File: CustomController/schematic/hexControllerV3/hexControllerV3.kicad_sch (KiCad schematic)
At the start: 48 parts, among them IC1 ESP32-S2-MINI-1-N4R2, IC2 IP5306, J1 USB_C_Receptacle_USB2.0_16P, J2 Battery, J3 Switch1, J4 Switch2, J5 Switch3, J6 Switch4, J7 Battery, SW1 RotaryEncoder_Switch, SW2 SW_DIP_x01, SW3 SW_DIP_x01, SW4 SW_DIP_x01, SW5 SW_DIP_x01, SW6 SW_DIP_x01, U2 AMS1117-3.3

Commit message: Improved PCB design
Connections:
- net Switch1: now also IC1.19 (IO15); no longer IC1.18 (IO14)
- net Switch2: now also IC1.18 (IO14); no longer IC1.19 (IO15)
- net button1: now also IC1.33 (IO37)
- net button2: now also IC1.34 (IO38)
- net button3: now also IC1.35 (IO39)
- net button4: now also IC1.36 (IO40)
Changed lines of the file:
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@@
+		)
+	)
+	(global_label "button4"
+		(shape input)
+		(at 184.15 115.57 180)
+		(fields_autoplaced yes)
+		(effects
+			(font
+				(size 1.27 1.27)
+			)
+			(justify right)
+		)
+		(property "Intersheetrefs" "${INTERSHEET_REFS}"
+			(at 173.9079 115.57 0)
+			(effects
+				(font
+					(size 1.27 1.27)
+				)
+				(justify right)
+				(hide yes)
+			)
 		)
 	)
@@
 		)
 	)
+	(global_label "button2"
+		(shape input)
+		(at 184.15 110.49 180)
+		(fields_autoplaced yes)
+		(effects
+			(font
+				(size 1.27 1.27)
+			)
+			(justify right)
+		)
+		(property "Intersheetrefs" "${INTERSHEET_REFS}"
+			(at 173.9079 110.49 0)
+			(effects
+				(font
+					(size 1.27 1.27)
+				)
+				(justify right)
+				(hide yes)
+			)
+		)
+	)
 	(global_label "Switch3"
 		(shape input)
@@
 		)
 	)
+	(global_label "button3"
+		(shape input)
+		(at 184.15 113.03 180)
+		(fields_autoplaced yes)
+		(effects
+			(font
+				(size 1.27 1.27)
+			)
+			(justify right)
+		)
+		(property "Intersheetrefs" "${INTERSHEET_REFS}"
+			(at 173.9079 113.03 0)
+			(effects
+				(font
+					(size 1.27 1.27)
+				)
+				(justify right)
+				(hide yes)
+			)
+		)
+	)
 	(global_label "DIN"
 		(shape input)
@@
 		)
 	)
+	(global_label "button1"
+		(shape input)
+		(at 184.15 107.95 180)
+		(fields_autoplaced yes)
+		(effects
+			(font
+				(size 1.27 1.27)
+			)
+			(justify right)
+		)
+		(property "Intersheetrefs" "${INTERSHEET_REFS}"
+			(at 173.9079 107.95 0)
+			(effects
+				(font
+					(size 1.27 1.27)
+				)
+				(justify right)
+				(hide yes)
+			)
+		)
+	)
 	(global_label "D-"
 		(shape input)
@@
 	(global_label "Switch2"
 		(shape input)
+		(at 172.72 69.85 180)
+		(fields_autoplaced yes)
+		(effects
+			(font
+				(size 1.27 1.27)
+			)
+			(justify right)
+		)
+		(property "Intersheetrefs" "${INTERSHEET_REFS}"
+			(at 162.4172 69.85 0)
+			(effects
+				(font
+					(size 1.27 1.27)
+				)
+				(justify right)
+				(hide yes)
+			)
+		)
+	)
+	(global_label "EncoderSW"
+		(shape input)
+		(at 157.48 52.07 180)
+		(fields_autoplaced yes)
+		(effects
+			(font
+				(size 1.27 1.27)
+			)
+			(justify right)
+		)
+		(property "Intersheetrefs" "${INTERSHEET_REFS}"
+			(at 145.8468 52.07 0)
+			(effects
+				(font
+					(size 1.27 1.27)
+				)
+				(justify right)
+				(hide yes)
+			)
+		)
+	)
+	(global_label "BOOT"
+		(shape input)
+		(at 184.15 34.29 180)
+		(fields_autoplaced yes)
+		(effects
+			(font
+				(size 1.27 1.27)
+			)
+			(justify right)
+		)
+		(property "Intersheetrefs" "${INTERSHEET_REFS}"
+			(at 176.2662 34.29 0)
+			(effects
+				(font
+					(size 1.27 1.27)
+				)
+				(justify right)
+				(hide yes)
+			)
+		)
+	)
+	(global_label "Joy1Y"
+		(shape input)
+		(at 158.75 36.83 180)
+		(fields_autoplaced yes)
+		(effects
+			(font
+				(size 1.27 1.27)
+			)
+			(justify right)
+		)
+		(property "Intersheetrefs" "${INTERSHEET_REFS}"
+			(at 150.2616 36.83 0)
+			(effects
+				(font
+					(size 1.27 1.27)
+				)
+				(justify right)
+				(hide yes)
+			)
+		)
+	)
+	(global_label "Joy1X"
+		(shape input)
+		(at 158.75 39.37 180)
+		(fields_autoplaced yes)
+		(effects
+			(font
+				(size 1.27 1.27)
+			)
+			(justify right)
+		)
+		(property "Intersheetrefs" "${INTERSHEET_REFS}"
+			(at 150.3825 39.37 0)
+			(effects
+				(font
+					(size 1.27 1.27)
+				)
+				(justify right)
+				(hide yes)
+			)
+		)
+	)
+	(global_label "EN"
+		(shape input)
+		(at 59.69 256.54 180)
+		(fields_autoplaced yes)
+		(effects
+			(font
+				(size 1.27 1.27)
+			)
+			(justify right)
+		)
+		(property "Intersheetrefs" "${INTERSHEET_REFS}"
+			(at 54.2253 256.54 0)
+			(effects
+				(font
+					(size 1.27 1.27)
+				)
+				(justify right)
+				(hide yes)
+			)
+		)
+	)
+	(global_label "DC"
+		(shape input)
+		(at 29.21 22.86 0)
+		(fields_autoplaced yes)
+		(effects
+			(font
+				(size 1.27 1.27)
+			)
+			(justify left)
+		)
+		(property "Intersheetrefs" "${INTERSHEET_REFS}"
+			(at 34.7352 22.86 0)
+			(effects
+				(font
+					(size 1.27 1.27)
+				)
+				(justify left)
+				(hide yes)
+			)
+		)
+	)
+	(global_label "Joy2Y"
+		(shape input)
+		(at 24.13 86.36 180)
+		(fields_autoplaced yes)
+		(effects
+			(font
+				(size 1.27 1.27)
+			)
+			(justify right)
+		)
+		(property "Intersheetrefs" "${INTERSHEET_REFS}"
+			(at 15.7625 86.36 0)
+			(effects
+				(font
+					(size 1.27 1.27)
+				)
+				(justify right)
+				(hide yes)
+			)
+		)
+	)
+	(global_label "Switch1"
+		(shape input)
 		(at 172.72 72.39 180)
 		(fields_autoplaced yes)
@@
 			(effects
 				(font
-					(size 1.27 1.27)
-				)
-				(justify right)
-				(hide yes)
-			)
-		)
-	)
-	(global_label "EncoderSW"
-		(shape input)
-		(at 157.48 52.07 180)
-		(fields_autoplaced yes)
-		(effects
-			(font
-				(size 1.27 1.27)
-			)
-			(justify right)
-		)
-		(property "Intersheetrefs" "${INTERSHEET_REFS}"
-			(at 145.8468 52.07 0)
-			(effects
-				(font
-					(size 1.27 1.27)
-				)
-				(justify right)
-				(hide yes)
-			)
-		)
-	)
-	(global_label "BOOT"
-		(shape input)
-		(at 184.15 34.29 180)
-		(fields_autoplaced yes)
-		(effects
-			(font
-				(size 1.27 1.27)
-			)
-			(justify right)
-		)
-		(property "Intersheetrefs" "${INTERSHEET_REFS}"
-			(at 176.2662 34.29 0)
-			(effects
-				(font
-					(size 1.27 1.27)
-				)
-				(justify right)
-				(hide yes)
-			)
-		)
-	)
-	(global_label "Joy1Y"
-		(shape input)
-		(at 158.75 36.83 180)
-		(fields_autoplaced yes)
-		(effects
-			(font
-				(size 1.27 1.27)
-			)
-			(justify right)
-		)
-		(property "Intersheetrefs" "${INTERSHEET_REFS}"
-			(at 150.2616 36.83 0)
-			(effects
-				(font
-					(size 1.27 1.27)
-				)
-				(justify right)
-				(hide yes)
-			)
-		)
-	)
-	(global_label "Joy1X"
-		(shape input)
-		(at 158.75 39.37 180)
-		(fields_autoplaced yes)
-		(effects
-			(font
-				(size 1.27 1.27)
-			)
-			(justify right)
-		)
-		(property "Intersheetrefs" "${INTERSHEET_REFS}"
-			(at 150.3825 39.37 0)
-			(effects
-				(font
-					(size 1.27 1.27)
-				)
-				(justify right)
-				(hide yes)
-			)
-		)
-	)
-	(global_label "EN"
-		(shape input)
-		(at 59.69 256.54 180)
-		(fields_autoplaced yes)
-		(effects
-			(font
-				(size 1.27 1.27)
-			)
-			(justify right)
-		)
-		(property "Intersheetrefs" "${INTERSHEET_REFS}"
-			(at 54.2253 256.54 0)
-			(effects
-				(font
-					(size 1.27 1.27)
-				)
-				(justify right)
-				(hide yes)
-			)
-		)
-	)
-	(global_label "DC"
-		(shape input)
-		(at 29.21 22.86 0)
-		(fields_autoplaced yes)
-		(effects
-			(font
-				(size 1.27 1.27)
-			)
-			(justify left)
-		)
-		(property "Intersheetrefs" "${INTERSHEET_REFS}"
-			(at 34.7352 22.86 0)
-			(effects
-				(font
-					(size 1.27 1.27)
-				)
-				(justify left)
-				(hide yes)
-			)
-		)
-	)
-	(global_label "Joy2Y"
-		(shape input)
-		(at 24.13 86.36 180)
-		(fields_autoplaced yes)
-		(effects
-			(font
-				(size 1.27 1.27)
-			)
-			(justify right)
-		)
-		(property "Intersheetrefs" "${INTERSHEET_REFS}"
-			(at 15.7625 86.36 0)
-			(effects
-				(font
-					(size 1.27 1.27)
-				)
-				(justify right)
-				(hide yes)
-			)
-		)
-	)
-	(global_label "Switch1"
-		(shape input)
-		(at 172.72 69.85 180)
-		(fields_autoplaced yes)
-		(effects
-			(font
-				(size 1.27 1.27)
-			)
-			(justify right)
-		)
-		(property "Intersheetrefs" "${INTERSHEET_REFS}"
-			(at 162.4172 69.85 0)
-			(effects
-				(font

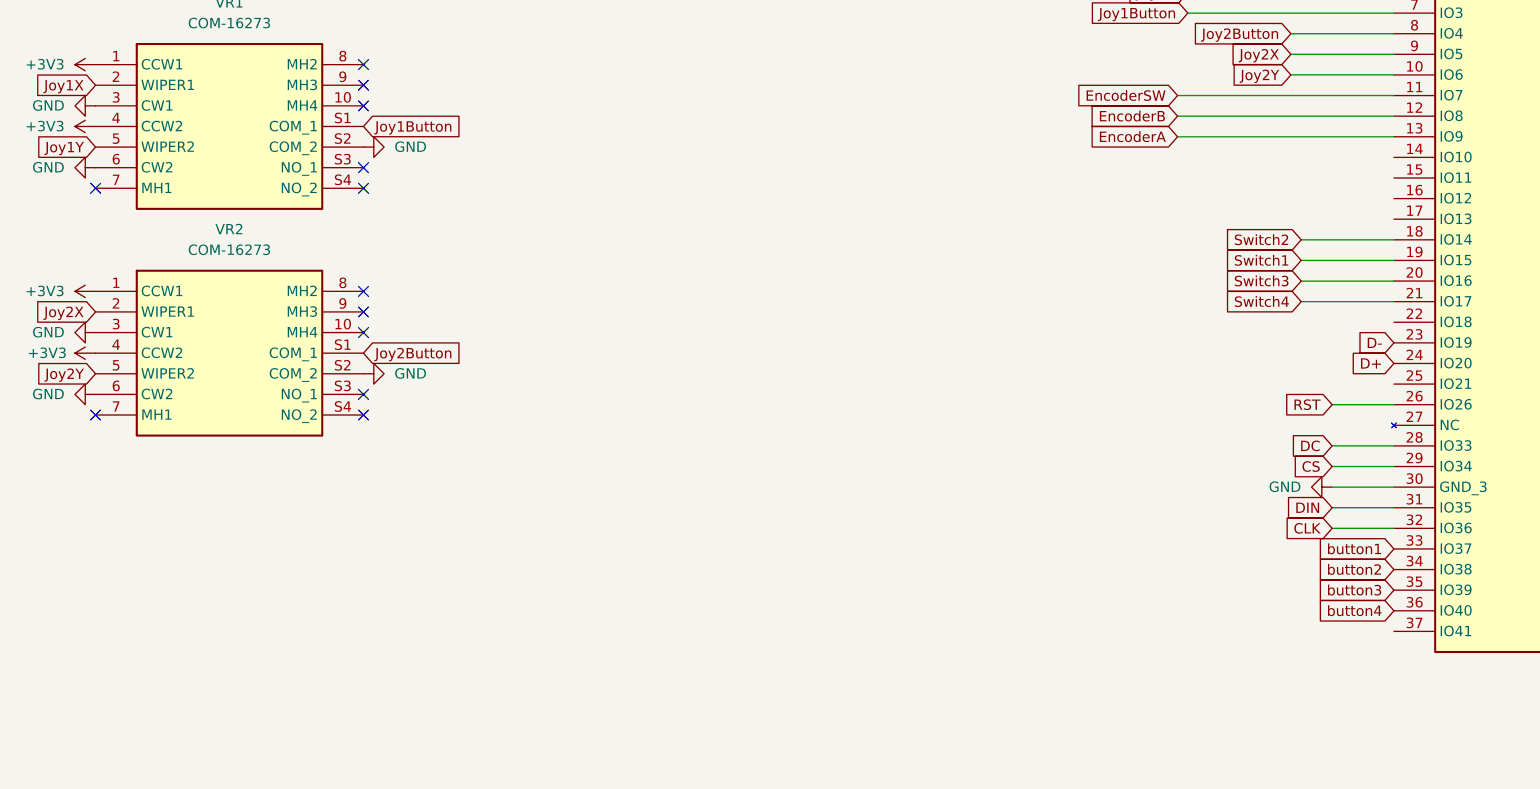
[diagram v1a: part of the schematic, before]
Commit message: Altered controller schematic
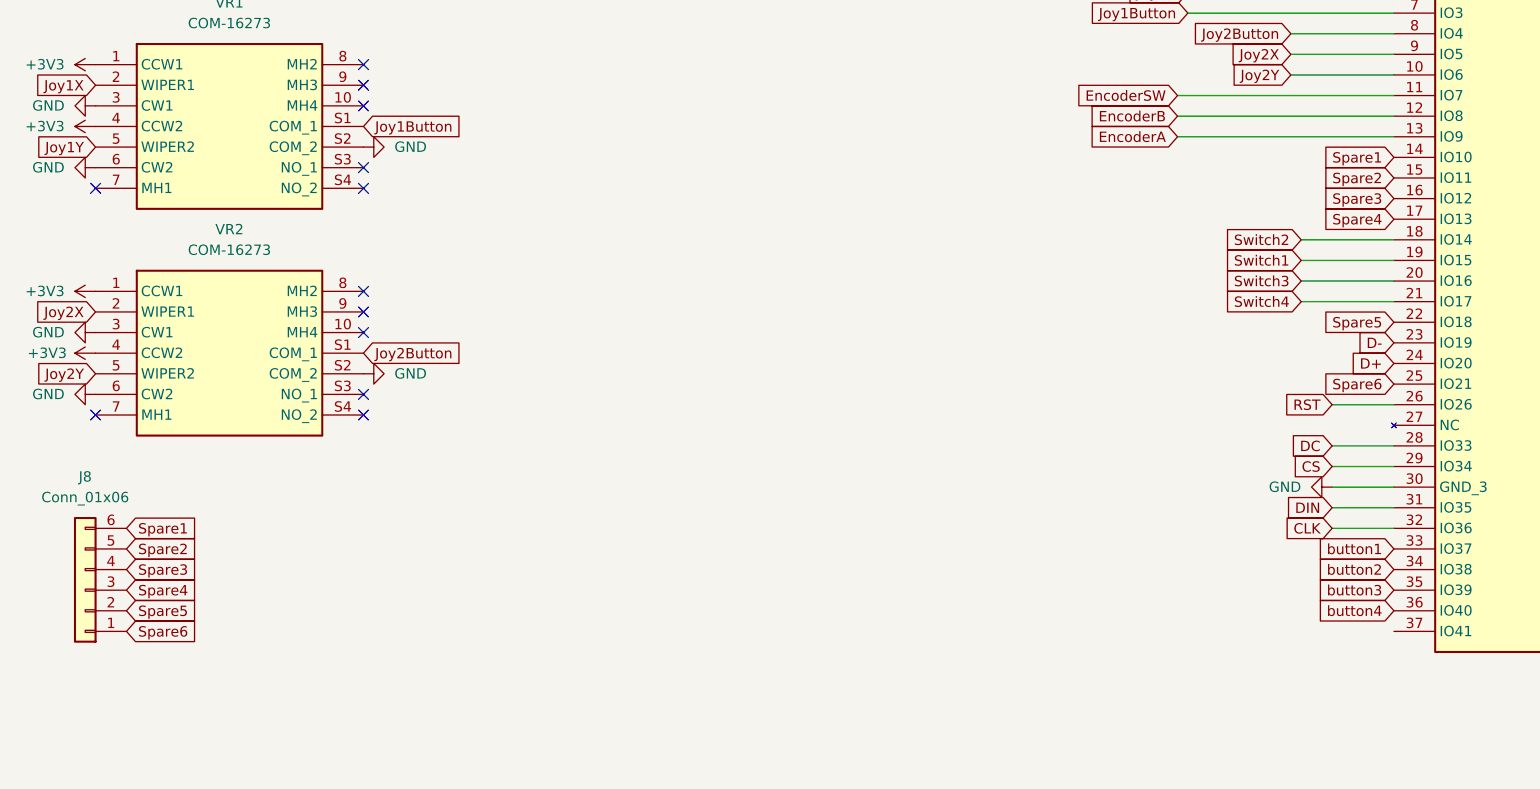
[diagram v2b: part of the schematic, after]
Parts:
- added J8: Conn_01x06, Connector_PinHeader_2.54mm:PinHeader_1x06_P2.54mm_Vertical, symbol Connector_Generic:Conn_01x06
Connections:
- net Spare1: now reaches IC1.14 (IO10)
- net Spare1: now also J8.6 (Pin_6)
- net Spare2: now reaches IC1.15 (IO11)
- net Spare2: now also J8.5 (Pin_5)
- net Spare3: now reaches IC1.16 (IO12)
- net Spare3: now also J8.4 (Pin_4)
- net Spare4: now reaches IC1.17 (IO13)
- net Spare4: now also J8.3 (Pin_3)
- net Spare5: now reaches IC1.22 (IO18)
- net Spare5: now also J8.2 (Pin_2)
- net Spare6: now reaches IC1.25 (IO21)
- net Spare6: now also J8.1 (Pin_1)

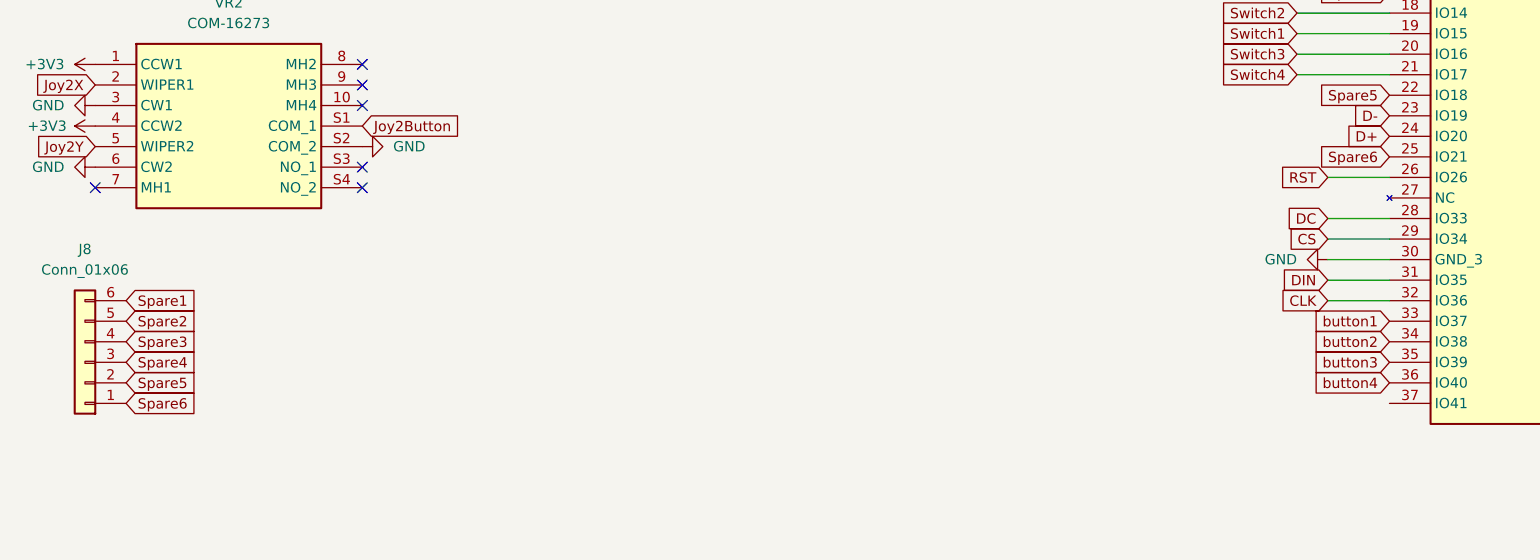
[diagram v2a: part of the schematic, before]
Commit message: Corrected pin config for schematic
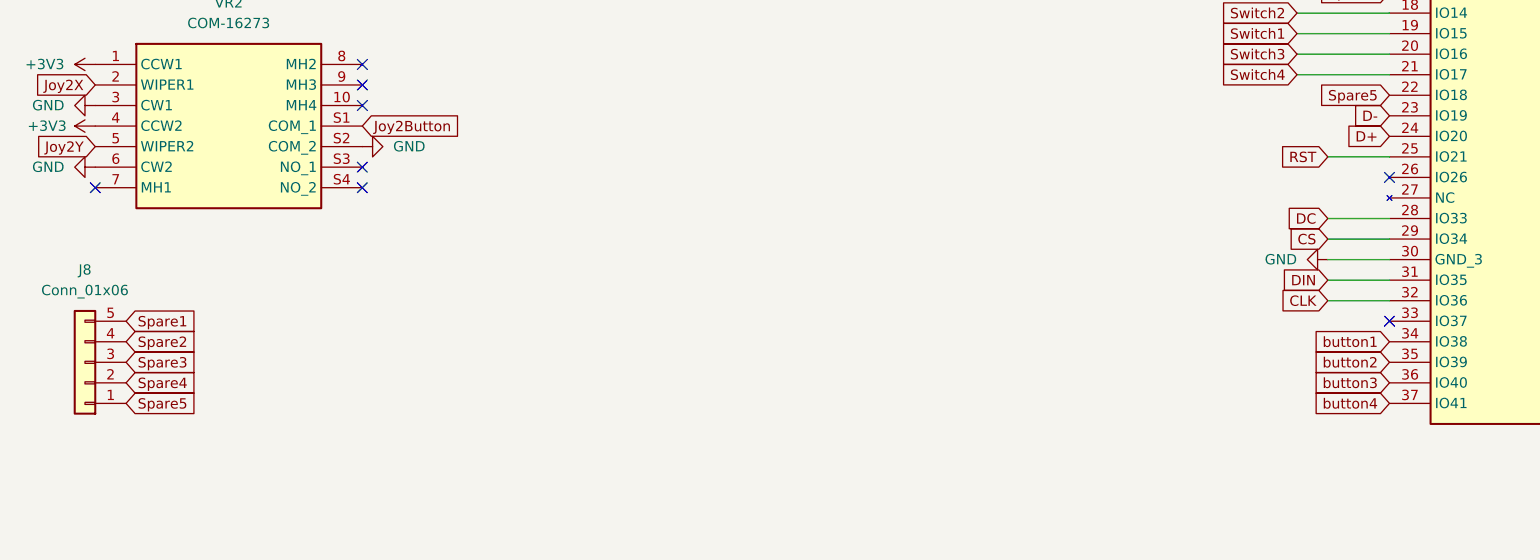
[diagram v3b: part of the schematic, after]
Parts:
- J8: footprint Connector_PinHeader_2.54mm:PinHeader_1x06_P2.54mm_Vertical -> Connector_PinHeader_2.54mm:PinHeader_1x05_P2.54mm_Vertical; symbol Connector_Generic:Conn_01x06 -> Connector_Generic:Conn_01x05
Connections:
- net RST: now also IC1.25 (IO21); no longer IC1.26 (IO26)
- net Spare1: now also J8.5 (Pin_5); no longer J8.6 (Pin_6)
- net Spare2: now also J8.4 (Pin_4); no longer J8.5 (Pin_5)
- net Spare3: now also J8.3 (Pin_3); no longer J8.4 (Pin_4)
- net Spare4: now also J8.2 (Pin_2); no longer J8.3 (Pin_3)
- net Spare5: now also J8.1 (Pin_1); no longer J8.2 (Pin_2)
- net button1: now also IC1.34 (IO38); no longer IC1.33 (IO37)
- net button2: now also IC1.35 (IO39); no longer IC1.34 (IO38)
- net button3: now also IC1.36 (IO40); no longer IC1.35 (IO39)
- net button4: now also IC1.37 (IO41); no longer IC1.36 (IO40)
- removed net Spare6: IC1.25 (IO21), J8.1 (Pin_1)
- no-connect marks 14 -> 16
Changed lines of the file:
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@@
 	)
 	(no_connect
+		(at 184.15 107.95)
+	)
+	(no_connect
 		(at 57.15 88.9)
 	)
@@
 	)
 	(no_connect
+		(at 184.15 90.17)
+	)
+	(no_connect
 		(at 57.15 76.2)
 	)
@@
 	(wire
 		(pts
+			(xy 176.53 87.63) (xy 184.15 87.63)
+		)
+		(stroke
+			(width 0)
+			(type default)
+		)
+	)
+	(wire
+		(pts
 			(xy 217.17 57.15) (xy 218.44 57.15)
 		)
@@
 	(wire
 		(pts
-			(xy 176.53 90.17) (xy 184.15 90.17)
-		)
-		(stroke
-			(width 0)
-			(type default)
-		)
-	)
-	(wire
-		(pts
 			(xy 384.81 210.82) (xy 388.62 210.82)
 		)
@@
 	(global_label "Spare2"
 		(shape input)
-		(at 27.94 107.95 0)
+		(at 27.94 110.49 0)
 		(fields_autoplaced yes)
 		(effects
@@
 		)
 		(property "Intersheetrefs" "${INTERSHEET_REFS}"
-			(at 37.517 107.95 0)
+			(at 37.517 110.49 0)
 			(effects
 				(font
@@
 	(global_label "button4"
 		(shape input)
-		(at 184.15 115.57 180)
+		(at 184.15 118.11 180)
 		(fields_autoplaced yes)
 		(effects
@@
 		)
 		(property "Intersheetrefs" "${INTERSHEET_REFS}"
-			(at 173.9079 115.57 0)
+			(at 173.9079 118.11 0)
 			(effects
 				(font
@@
 	(global_label "button2"
 		(shape input)
-		(at 184.15 110.49 180)
+		(at 184.15 113.03 180)
 		(fields_autoplaced yes)
 		(effects
@@
 		)
 		(property "Intersheetrefs" "${INTERSHEET_REFS}"
-			(at 173.9079 110.49 0)
+			(at 173.9079 113.03 0)
 			(effects
 				(font
@@
 		)
 	)
-	(global_label "Spare6"
-		(shape input)
-		(at 27.94 118.11 0)
-		(fields_autoplaced yes)
-		(effects
-			(font
-				(size 1.27 1.27)
-			)
-			(justify left)
-		)
-		(property "Intersheetrefs" "${INTERSHEET_REFS}"
-			(at 37.517 118.11 0)
-			(effects
-				(font
-					(size 1.27 1.27)
-				)
-				(justify left)
-				(hide yes)
-			)
-		)
-	)
 	(global_label "Switch3"
 		(shape input)
@@
 	(global_label "button3"
 		(shape input)
-		(at 184.15 113.03 180)
+		(at 184.15 115.57 180)
 		(fields_autoplaced yes)
 		(effects
@@
 		)
 		(property "Intersheetrefs" "${INTERSHEET_REFS}"
-			(at 173.9079 113.03 0)
+			(at 173.9079 115.57 0)
 			(effects
 				(font
@@
 	(global_label "Spare1"
 		(shape input)
-		(at 27.94 105.41 0)
+		(at 27.94 107.95 0)
 		(fields_autoplaced yes)
 		(effects
@@
 		)
 		(property "Intersheetrefs" "${INTERSHEET_REFS}"
-			(at 37.517 105.41 0)
+			(at 37.517 107.95 0)
 			(effects
 				(font
@@
 	(global_label "RST"
 		(shape input)
-		(at 176.53 90.17 180)
+		(at 176.53 87.63 180)
 		(fields_autoplaced yes)
 		(effects
@@
 		)
 		(property "Intersheetrefs" "${INTERSHEET_REFS}"
-			(at 170.0977 90.17 0)
+			(at 170.0977 87.63 0)
 			(effects
 				(font
@@
 	(global_label "Spare3"
 		(shape input)
-		(at 27.94 110.49 0)
+		(at 27.94 113.03 0)
 		(fields_autoplaced yes)
 		(effects
@@
 		)
 		(property "Intersheetrefs" "${INTERSHEET_REFS}"
-			(at 37.517 110.49 0)
+			(at 37.517 113.03 0)
 			(effects
 				(font
@@
 	(global_label "button1"
 		(shape input)
-		(at 184.15 107.95 180)
+		(at 184.15 110.49 180)
 		(fields_autoplaced yes)
 		(effects
@@
 		)
 		(property "Intersheetrefs" "${INTERSHEET_REFS}"
-			(at 173.9079 107.95 0)
+			(at 173.9079 110.49 0)
 			(effects
 				(font
@@
 		)
 	)
-	(global_label "Spare6"
-		(shape input)
-		(at 184.15 87.63 180)
-		(fields_autoplaced yes)
-		(effects
-			(font
-				(size 1.27 1.27)
-			)
-			(justify right)
-		)
-		(property "Intersheetrefs" "${INTERSHEET_REFS}"
-			(at 174.573 87.63 0)
-			(effects
-				(font
-					(size 1.27 1.27)
-				)
-				(justify right)
-				(hide yes)
-			)
-		)
-	)
 	(global_label "DC"
 		(shape input)
@@
 	(global_label "Spare5"
 		(shape input)
-		(at 27.94 115.57 0)
+		(at 27.94 118.11 0)
 		(fields_autoplaced yes)
 		(effects
@@
 		)
 		(property "Intersheetrefs" "${INTERSHEET_REFS}"
-			(at 37.517 115.57 0)
+			(at 37.517 118.11 0)
 			(effects
 				(font
@@
 	(global_label "Spare4"
 		(shape input)
-		(at 27.94 113.03 0)
+		(at 27.94 115.57 0)
 		(fields_autoplaced yes)
 		(effects
@@
 		)
 		(property "Intersheetrefs" "${INTERSHEET_REFS}"
-			(at 37.517 113.03 0)
+			(at 37.517 115.57 0)
 			(effects
 				(font
@@
 	)
 	(symbol
-		(lib_id "Connector_Generic:Conn_01x06")
+		(lib_id "Connector_Generic:Conn_01x05")
 		(at 22.86 113.03 180)
 		(unit 1)
@@
 		(fields_autoplaced yes)
 		(property "Reference" "J8"
-			(at 22.86 99.06 0)
+			(at 22.86 101.6 0)
 			(effects
 				(font
@@
 		)
 		(property "Value" "Conn_01x06"
-			(at 22.86 101.6 0)
+			(at 22.86 104.14 0)
 			(effects
 				(font
@@
 			)
 		)
-		(property "Footprint" "Connector_PinHeader_2.54mm:PinHeader_1x06_P2.54mm_Vertical"
+		(property "Footprint" "Connector_PinHeader_2.54mm:PinHeader_1x05_P2.54mm_Vertical"
 			(at 22.86 113.03 0)
 			(effects
@@
 			)
 		)
-		(property "Description" "Generic connector, single row, 01x06, script generated (kicad-library-utils/schlib/autogen/connector/)"
+		(property "Description" "Generic connector, single row, 01x05, script generated (kicad-library-utils/schlib/autogen/connector/)"
 			(at 22.86 113.03 0)
 			(effects
@@
 		(pin "5"
 		)
-		(pin "6"
-		)
 		(pin "4"
